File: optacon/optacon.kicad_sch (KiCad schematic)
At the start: 12 parts, among them J1 Conn_01x12, U1 HV528, U2 HV528

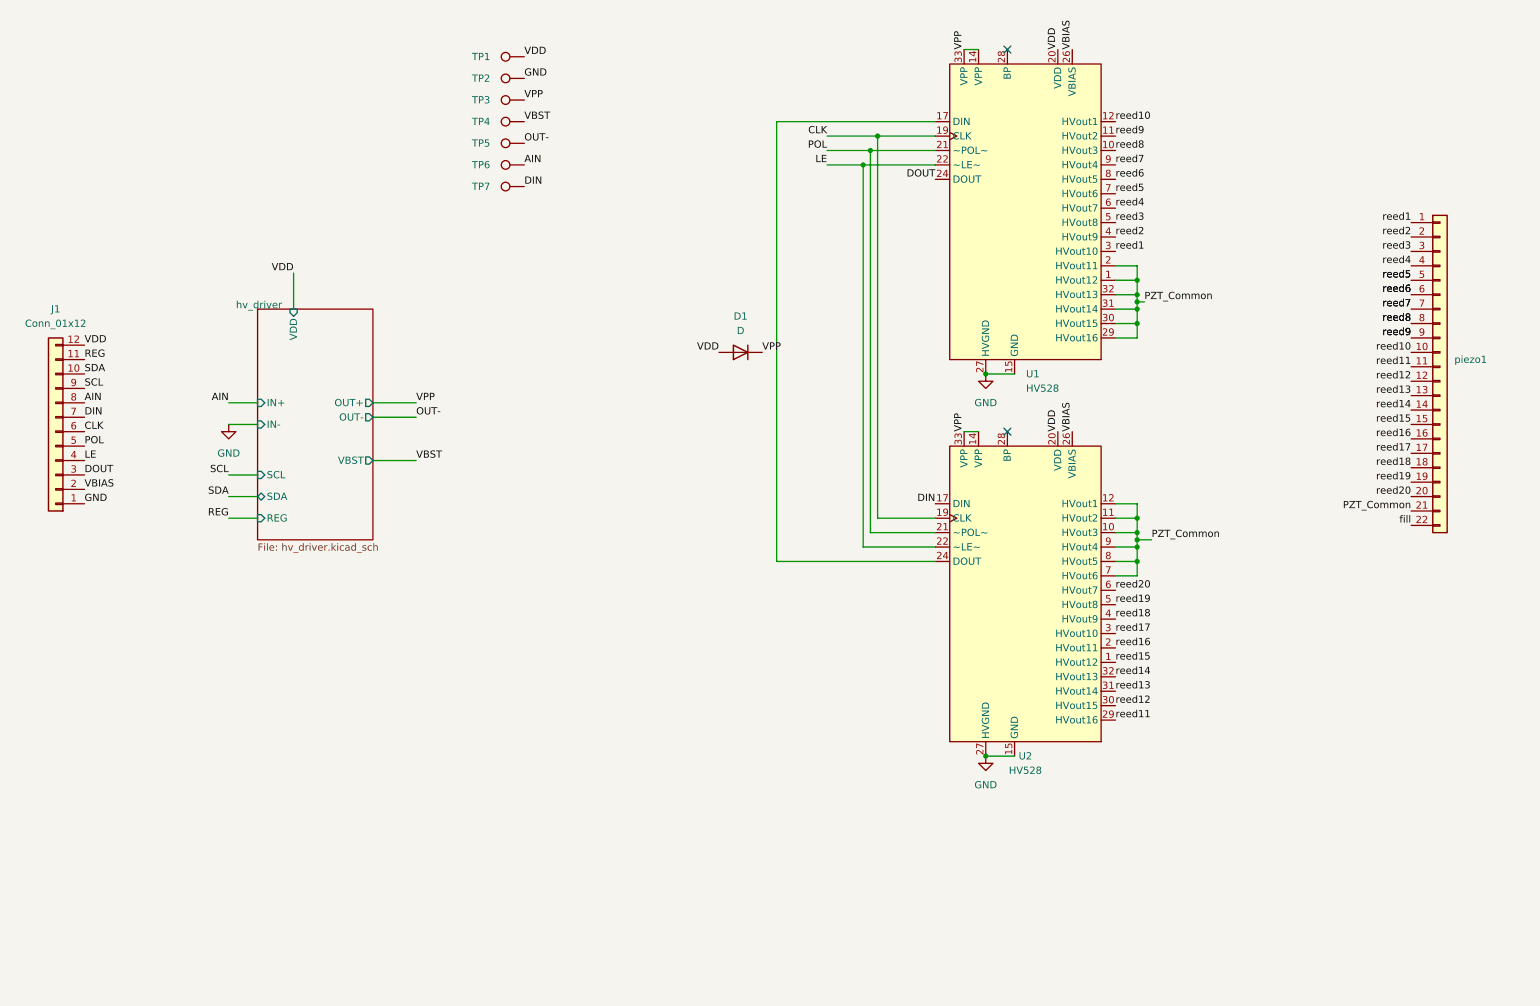
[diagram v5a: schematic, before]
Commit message: hierarchical sheet for shift registers
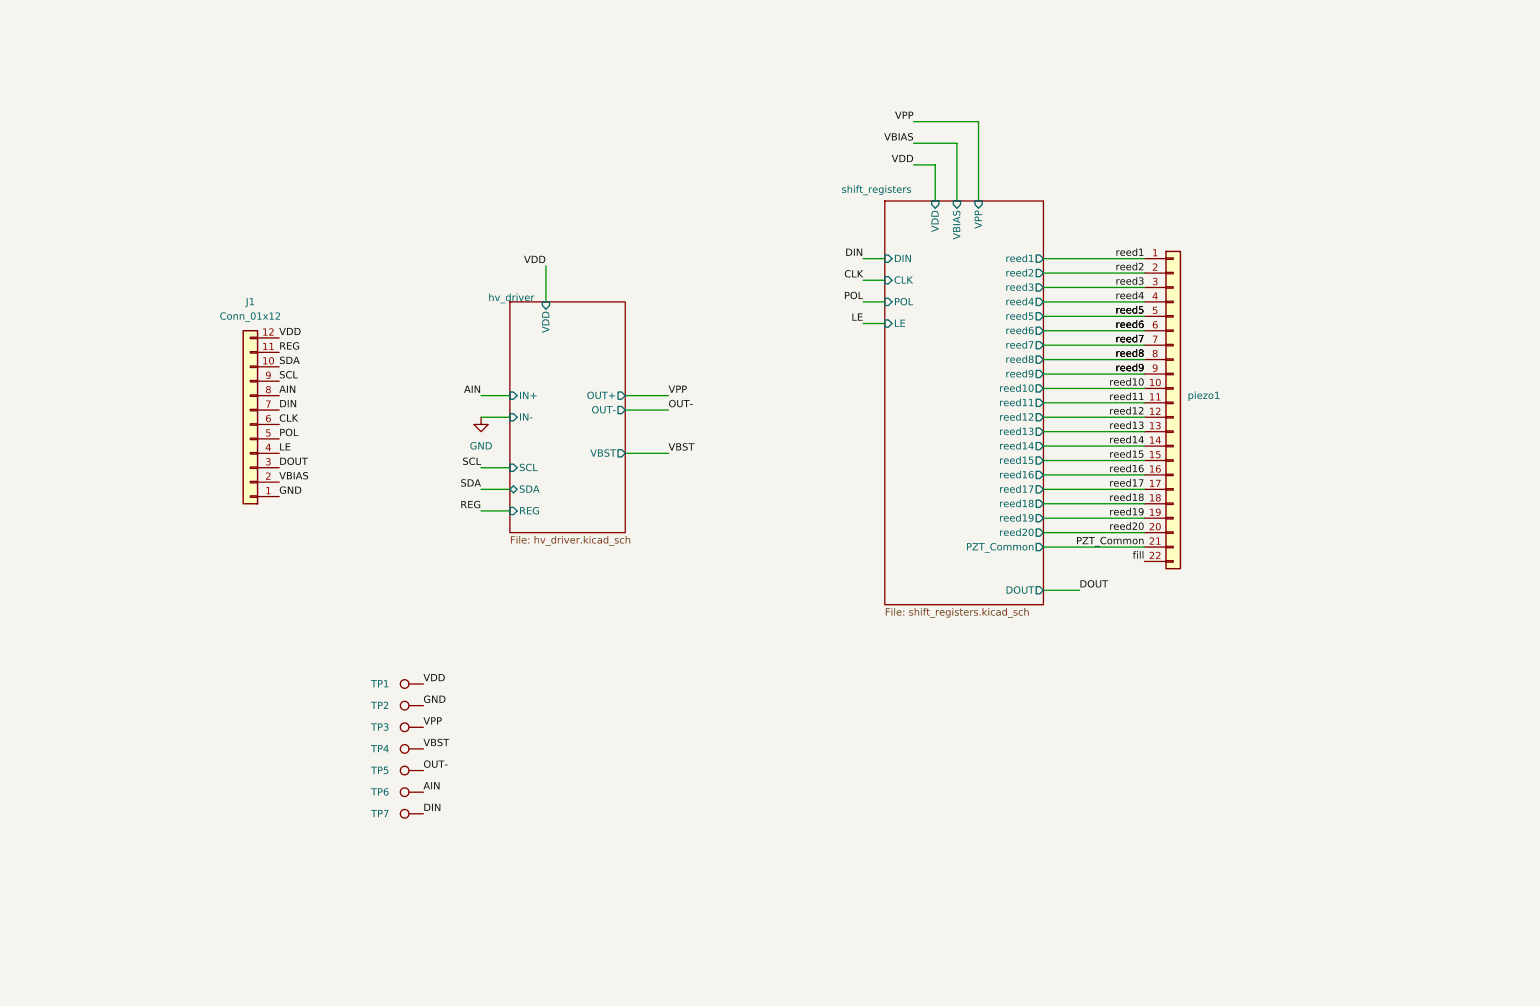
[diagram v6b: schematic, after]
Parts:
- removed D1: D, Diode_SMD:D_SOD-123F, symbol Device:D
- removed U1, U2: HV528, Package_DFN_QFN:HVQFN-32-1EP_5x5mm_P0.5mm_EP3.1x3.1mm, symbol microchip_hv:HV528
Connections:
- no-connect marks 2 -> 0
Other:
- added sheet shift_registers (shift_registers.kicad_sch)
- moved on the sheet: J1, TP1, TP2, TP3, TP4, TP5, TP6, TP7, piezo1

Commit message: test points
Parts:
- added TP10, TP11, TP12, TP13, TP14, TP15, TP8, TP9: TestPoint, TestPoint:TestPoint_Pad_D1.0mm, symbol Connector:TestPoint
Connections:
- net CLK: now also TP12.1
- net DOUT: now also TP8.1
- net LE: now also TP14.1
- net POL: now also TP13.1
- net REG: now also TP11.1
- net SCL: now also TP10.1
- net SDA: now also TP9.1
- net VBIAS: now also TP15.1
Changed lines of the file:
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@@
+    (effects (font (size 1.27 1.27)) (justify left bottom))
+  )
+  (label "VBIAS" (at 88.9 190.5 0)
     (effects (font (size 1.27 1.27)) (justify left bottom))
   )
@@
     (effects (font (size 1.27 1.27)) (justify right bottom))
   )
+  (label "SCL" (at 88.9 171.45 0)
+    (effects (font (size 1.27 1.27)) (justify left bottom))
+  )
   (label "POL" (at 63.5 93.98 0)
     (effects (font (size 1.27 1.27)) (justify left bottom))
@@
     (effects (font (size 1.27 1.27)) (justify left bottom))
   )
+  (label "DOUT" (at 88.9 163.83 0)
+    (effects (font (size 1.27 1.27)) (justify left bottom))
+  )
+  (label "CLK" (at 88.9 179.07 0)
+    (effects (font (size 1.27 1.27)) (justify left bottom))
+  )
   (label "DIN" (at 166.37 62.23 180)
     (effects (font (size 1.27 1.27)) (justify right bottom))
@@
     (effects (font (size 1.27 1.27)) (justify right bottom))
   )
+  (label "LE" (at 88.9 186.69 0)
+    (effects (font (size 1.27 1.27)) (justify left bottom))
+  )
   (label "OUT-" (at 132.08 88.9 0)
     (effects (font (size 1.27 1.27)) (justify left bottom))
   )
+  (label "POL" (at 88.9 182.88 0)
+    (effects (font (size 1.27 1.27)) (justify left bottom))
+  )
+  (label "REG" (at 88.9 175.26 0)
+    (effects (font (size 1.27 1.27)) (justify left bottom))
+  )
   (label "VBST" (at 88.9 148.59 0)
     (effects (font (size 1.27 1.27)) (justify left bottom))
@@
     (effects (font (size 1.27 1.27)) (justify right bottom))
   )
+  (label "SDA" (at 88.9 167.64 0)
+    (effects (font (size 1.27 1.27)) (justify left bottom))
+  )
   (label "DOUT" (at 204.47 120.65 0)
     (effects (font (size 1.27 1.27)) (justify left bottom))
@@
   (label "reed13" (at 215.9 92.71 180)
     (effects (font (size 1.27 1.27)) (justify right bottom))
+  )
+  (symbol (lib_id "Connector:TestPoint") (at 88.9 175.26 90) (unit 1)
+    (in_bom yes) (on_board yes)
+    (property "Reference" "TP11" (id 0) (at 81.28 175.26 90))
+    (property "Value" "TestPoint" (id 1) (at 95.25 175.26 90)
+      (effects (font (size 1.27 1.27)) hide)
+    )
+    (property "Footprint" "TestPoint:TestPoint_Pad_D1.0mm" (id 2) (at 88.9 170.18 0)
+      (effects (font (size 1.27 1.27)) hide)
+    )
+    (property "Datasheet" "~" (id 3) (at 88.9 170.18 0)
+      (effects (font (size 1.27 1.27)) hide)
+    )
+    (pin "1")
+  )
+  (symbol (lib_id "Connector:TestPoint") (at 88.9 171.45 90) (unit 1)
+    (in_bom yes) (on_board yes)
+    (property "Reference" "TP10" (id 0) (at 81.28 171.45 90))
+    (property "Value" "TestPoint" (id 1) (at 95.25 171.45 90)
+      (effects (font (size 1.27 1.27)) hide)
+    )
+    (property "Footprint" "TestPoint:TestPoint_Pad_D1.0mm" (id 2) (at 88.9 166.37 0)
+      (effects (font (size 1.27 1.27)) hide)
+    )
+    (property "Datasheet" "~" (id 3) (at 88.9 166.37 0)
+      (effects (font (size 1.27 1.27)) hide)
+    )
+    (pin "1")
   )
   (symbol (lib_id "Connector_Generic:Conn_01x22") (at 220.98 87.63 0) (unit 1)
@@
     (pin "9")
   )
+  (symbol (lib_id "Connector:TestPoint") (at 88.9 167.64 90) (unit 1)
+    (in_bom yes) (on_board yes)
+    (property "Reference" "TP9" (id 0) (at 81.28 167.64 90))
+    (property "Value" "TestPoint" (id 1) (at 95.25 167.64 90)
+      (effects (font (size 1.27 1.27)) hide)
+    )
+    (property "Footprint" "TestPoint:TestPoint_Pad_D1.0mm" (id 2) (at 88.9 162.56 0)
+      (effects (font (size 1.27 1.27)) hide)
+    )
+    (property "Datasheet" "~" (id 3) (at 88.9 162.56 0)
+      (effects (font (size 1.27 1.27)) hide)
+    )
+    (pin "1")
+  )
   (symbol (lib_id "Connector:TestPoint") (at 88.9 152.4 90) (unit 1)
     (in_bom yes) (on_board yes)
@@
     (pin "1")
   )
+  (symbol (lib_id "Connector:TestPoint") (at 88.9 163.83 90) (unit 1)
+    (in_bom yes) (on_board yes)
+    (property "Reference" "TP8" (id 0) (at 81.28 163.83 90))
+    (property "Value" "TestPoint" (id 1) (at 95.25 163.83 90)
+      (effects (font (size 1.27 1.27)) hide)
+    )
+    (property "Footprint" "TestPoint:TestPoint_Pad_D1.0mm" (id 2) (at 88.9 158.75 0)
+      (effects (font (size 1.27 1.27)) hide)
+    )
+    (property "Datasheet" "~" (id 3) (at 88.9 158.75 0)
+      (effects (font (size 1.27 1.27)) hide)
+    )
+    (pin "1")
+  )
+  (symbol (lib_id "Connector:TestPoint") (at 88.9 190.5 90) (unit 1)
+    (in_bom yes) (on_board yes)
+    (property "Reference" "TP15" (id 0) (at 81.28 190.5 90))
+    (property "Value" "TestPoint" (id 1) (at 95.25 190.5 90)
+      (effects (font (size 1.27 1.27)) hide)
+    )
+    (property "Footprint" "TestPoint:TestPoint_Pad_D1.0mm" (id 2) (at 88.9 185.42 0)
+      (effects (font (size 1.27 1.27)) hide)
+    )
+    (property "Datasheet" "~" (id 3) (at 88.9 185.42 0)
+      (effects (font (size 1.27 1.27)) hide)
+    )
+    (pin "1")
+  )
   (symbol (lib_id "Connector:TestPoint") (at 88.9 137.16 90) (unit 1)
     (in_bom yes) (on_board yes)
@@
     (pin "1")
   )
+  (symbol (lib_id "Connector:TestPoint") (at 88.9 186.69 90) (unit 1)
+    (in_bom yes) (on_board yes)
+    (property "Reference" "TP14" (id 0) (at 81.28 186.69 90))
+    (property "Value" "TestPoint" (id 1) (at 95.25 186.69 90)
+      (effects (font (size 1.27 1.27)) hide)
+    )
+    (property "Footprint" "TestPoint:TestPoint_Pad_D1.0mm" (id 2) (at 88.9 181.61 0)
+      (effects (font (size 1.27 1.27)) hide)
+    )
+    (property "Datasheet" "~" (id 3) (at 88.9 181.61 0)
+      (effects (font (size 1.27 1.27)) hide)
+    )
+    (pin "1")
+  )
   (symbol (lib_id "Connector:TestPoint") (at 88.9 148.59 90) (unit 1)
     (in_bom yes) (on_board yes)
@@
     )
     (property "Datasheet" "~" (id 3) (at 88.9 143.51 0)
+      (effects (font (size 1.27 1.27)) hide)
+    )
+    (pin "1")
+  )
+  (symbol (lib_id "Connector:TestPoint") (at 88.9 179.07 90) (unit 1)
+    (in_bom yes) (on_board yes)
+    (property "Reference" "TP12" (id 0) (at 81.28 179.07 90))
+    (property "Value" "TestPoint" (id 1) (at 95.25 179.07 90)
+      (effects (font (size 1.27 1.27)) hide)
+    )
+    (property "Footprint" "TestPoint:TestPoint_Pad_D1.0mm" (id 2) (at 88.9 173.99 0)
+      (effects (font (size 1.27 1.27)) hide)
+    )
+    (property "Datasheet" "~" (id 3) (at 88.9 173.99 0)
       (effects (font (size 1.27 1.27)) hide)
     )
@@
     (pin "9")
   )
+  (symbol (lib_id "Connector:TestPoint") (at 88.9 182.88 90) (unit 1)
+    (in_bom yes) (on_board yes)
+    (property "Reference" "TP13" (id 0) (at 81.28 182.88 90))
+    (property "Value" "TestPoint" (id 1) (at 95.25 182.88 90)
+      (effects (font (size 1.27 1.27)) hide)
+    )
+    (property "Footprint" "TestPoint:TestPoint_Pad_D1.0mm" (id 2) (at 88.9 177.8 0)
+      (effects (font (size 1.27 1.27)) hide)
+    )
+    (property "Datasheet" "~" (id 3) (at 88.9 177.8 0)
+      (effects (font (size 1.27 1.27)) hide)
+    )
+    (pin "1")
+  )
   (sheet (at 170.18 52.07) (size 27.94 71.12)
     (stroke (width 0.1524) (type solid) (color 0 0 0 0))
@@
       (reference "TP7") (unit 1) (value "TestPoint") (footprint "TestPoint:TestPoint_Pad_D1.0mm")
     )
+    (path "/3f787304-0f09-428f-9615-a178d53b5ed2"
+      (reference "TP8") (unit 1) (value "TestPoint") (footprint "TestPoint:TestPoint_Pad_D1.0mm")
+    )
+    (path "/2decf3cc-acf1-4c24-b86f-54bb47ef4745"
+      (reference "TP9") (unit 1) (value "TestPoint") (footprint "TestPoint:TestPoint_Pad_D1.0mm")
+    )
+    (path "/1aeddff5-502e-4ac0-9b06-6c6acb30e983"
+      (reference "TP10") (unit 1) (value "TestPoint") (footprint "TestPoint:TestPoint_Pad_D1.0mm")
+    )
+    (path "/04434920-f249-4b22-8306-90c69fb32842"
+      (reference "TP11") (unit 1) (value "TestPoint") (footprint "TestPoint:TestPoint_Pad_D1.0mm")
+    )
+    (path "/8723dc5d-47d0-453f-8eca-a53f7b3720d3"
+      (reference "TP12") (unit 1) (value "TestPoint") (footprint "TestPoint:TestPoint_Pad_D1.0mm")
+    )
+    (path "/fea54ca7-0fa6-4550-8a7f-f852771e86c1"
+      (reference "TP13") (unit 1) (value "TestPoint") (footprint "TestPoint:TestPoint_Pad_D1.0mm")
+    )
+    (path "/5b42eb09-d31e-47c9-9e9d-cb927ce3583c"
+      (reference "TP14") (unit 1) (value "TestPoint") (footprint "TestPoint:TestPoint_Pad_D1.0mm")
+    )
+    (path "/53c518ac-d58b-4fb6-ae0e-c81843505bf0"
+      (reference "TP15") (unit 1) (value "TestPoint") (footprint "TestPoint:TestPoint_Pad_D1.0mm")
+    )
     (path "/488f8d40-8ebd-4514-a509-75fe26050312/540fb909-0221-4a7a-ba3f-fa10c5679a0b"
